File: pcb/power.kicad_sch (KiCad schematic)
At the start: 6 parts

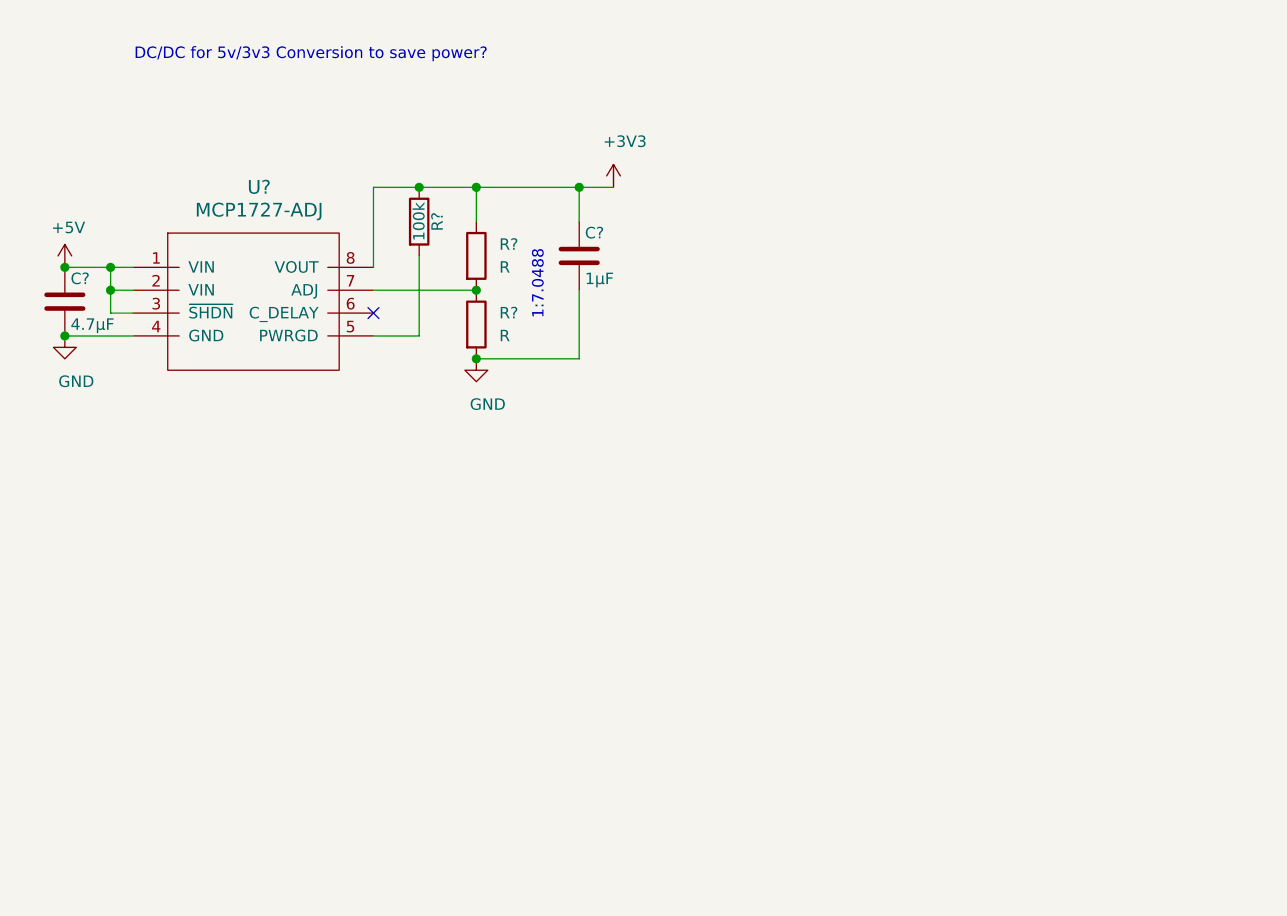
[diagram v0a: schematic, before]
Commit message: refinements; add ar1335 footprint
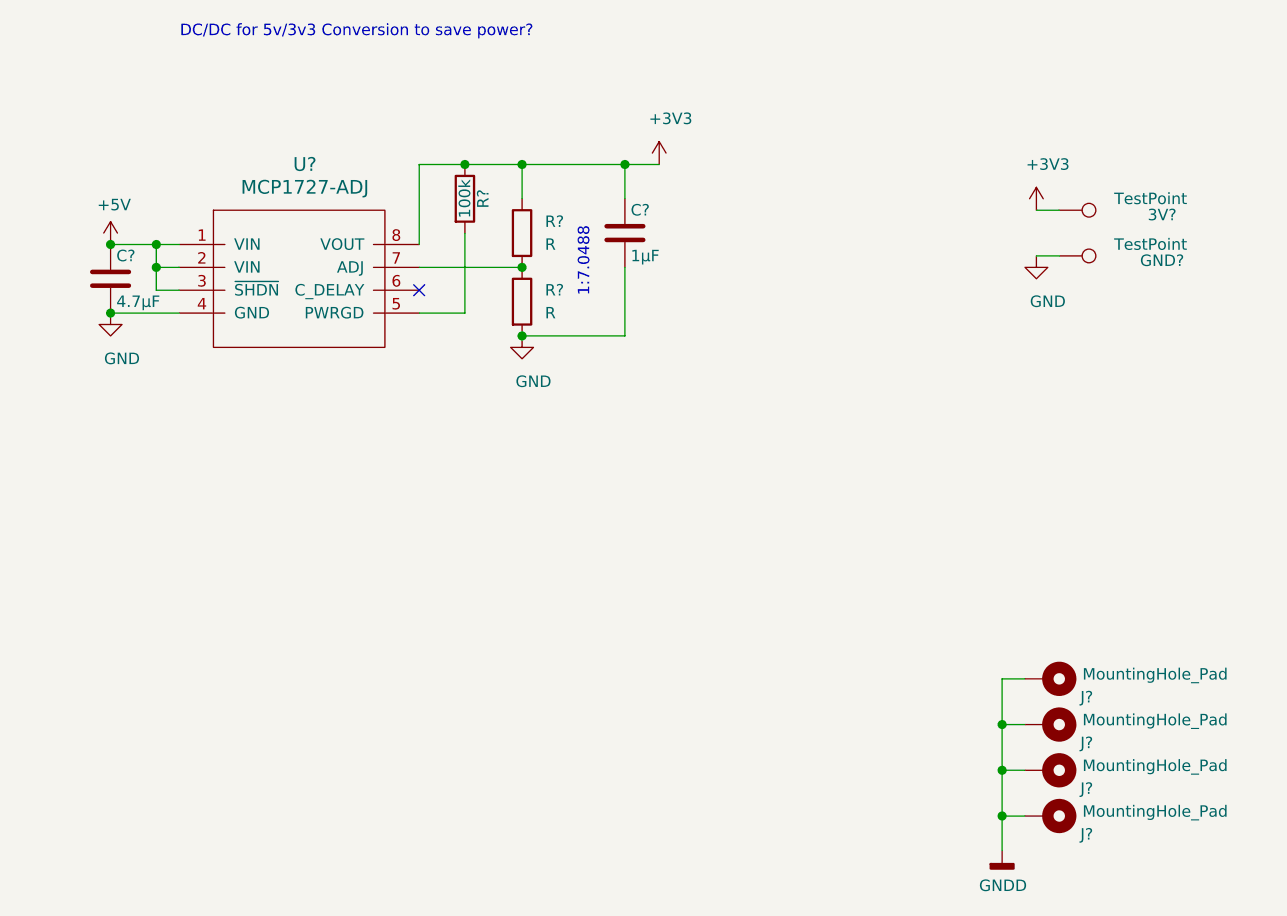
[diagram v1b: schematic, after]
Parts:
- added 3V?, GND?: TestPoint, Connectors_TestPoints:Test_Point_Pad_2.0x2.0mm, symbol Connector:TestPoint
- added J? (x4): MountingHole_Pad, Mounting_Holes:MountingHole_3.2mm_M3_Pad, symbol Mechanical:MountingHole_Pad
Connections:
- net +3V3: now also 3V?.1
- net GND: now also GND?.1
- new net GNDD: J?.1, J?.1, J?.1, J?.1
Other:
- moved on the sheet: C?, R?, U?

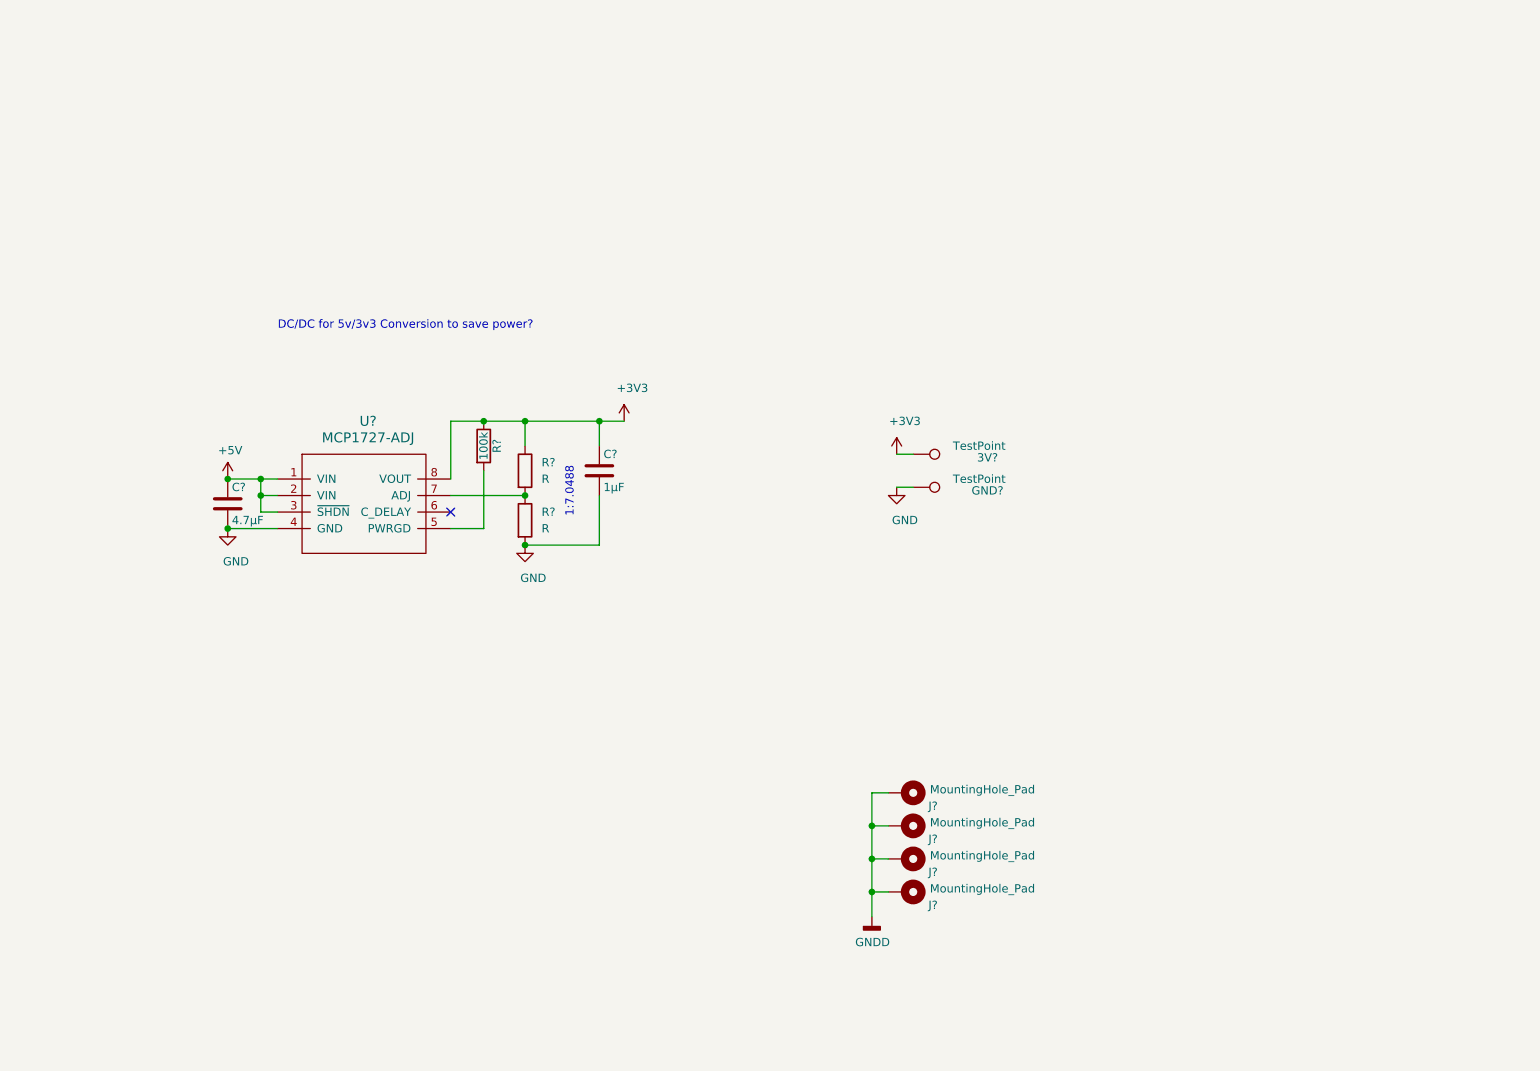
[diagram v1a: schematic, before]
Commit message: Change Plans: two image sensors
* Redo power management
* Add level shifters
* Intention to use both image sensors on the same board
* Add Pmod & LEDs
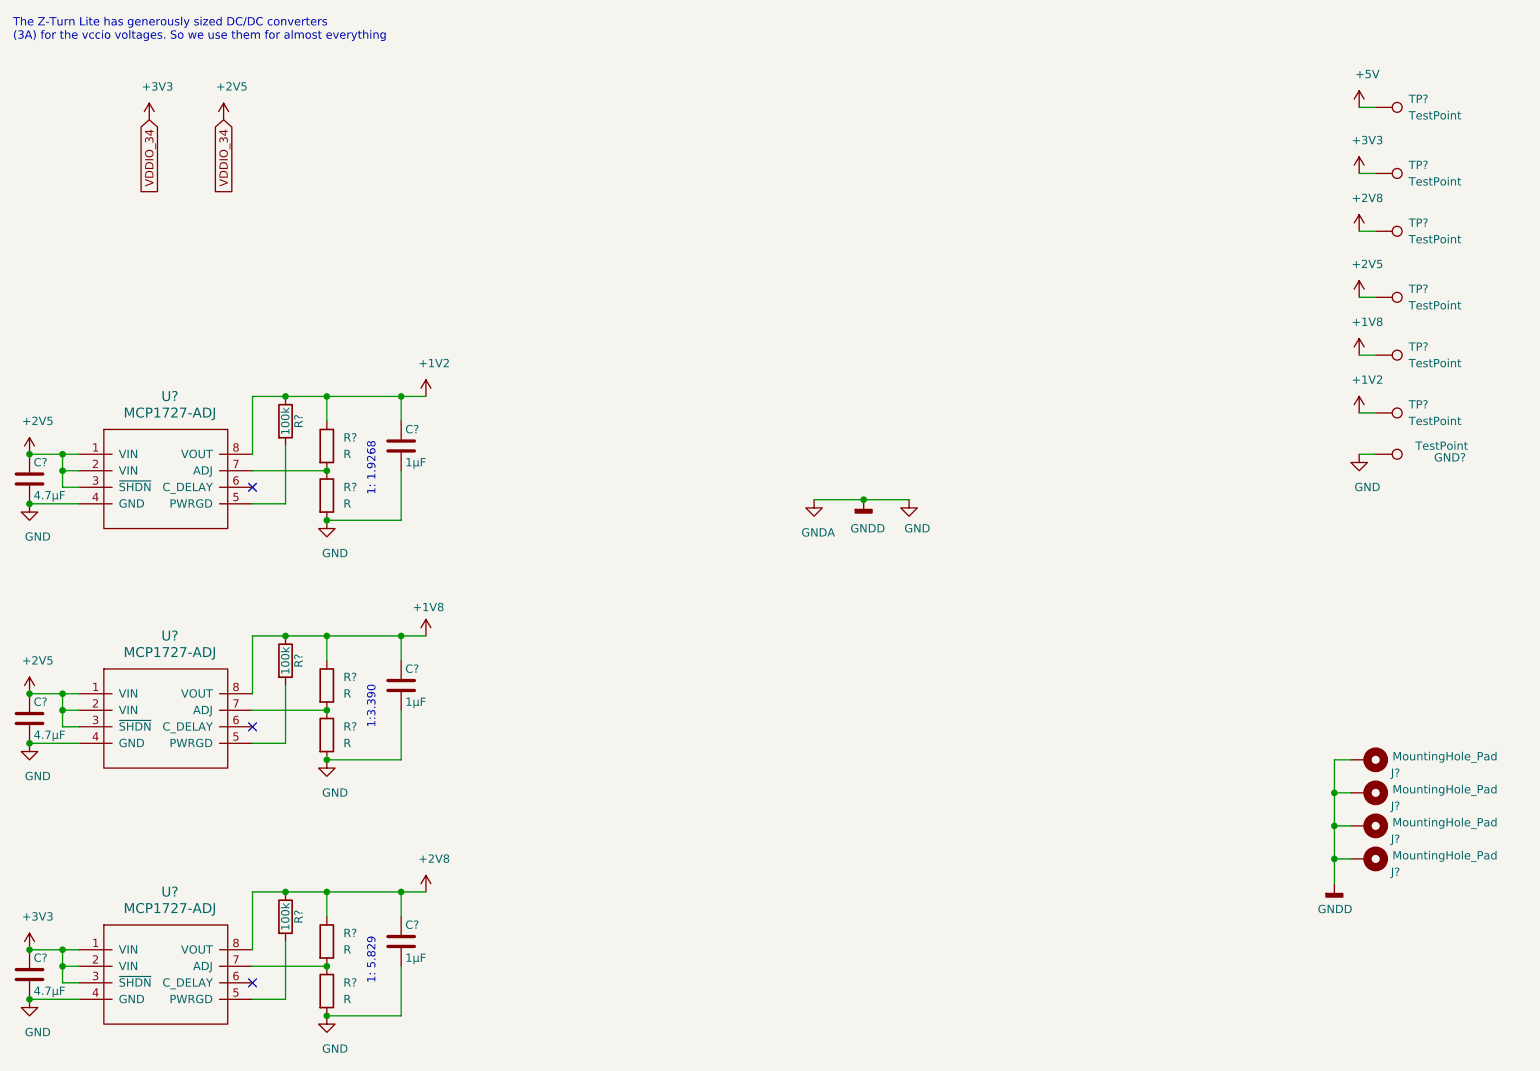
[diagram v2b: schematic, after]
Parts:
- removed 3V?: TestPoint, Connectors_TestPoints:Test_Point_Pad_2.0x2.0mm, symbol Connector:TestPoint
- removed C?: 4.7µF, Capacitors_SMD:C_0603_HandSoldering, symbol Device:C
- removed C?: 1µF, Capacitors_SMD:C_0402, symbol Device:C
- removed R?: 100k, Resistors_SMD:R_0603_HandSoldering, symbol Device:R
- removed R? (x2): R, symbol Device:R
- removed U?: MCP1727-ADJ, symbol parts:MCP1727-ADJ
- added C? (x3): 4.7µF, Capacitors_SMD:C_0603_HandSoldering, symbol Device:C
- added C? (x3): 1µF, Capacitors_SMD:C_0402, symbol Device:C
- added R? (x6): R, symbol Device:R
- added R? (x3): 100k, Resistors_SMD:R_0603_HandSoldering, symbol Device:R
- added TP? (x6): TestPoint, symbol Connector:TestPoint
- added U? (x3): MCP1727-ADJ, symbol parts:MCP1727-ADJ
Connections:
- net GNDD is gone; now on net GND: J?.1, J?.1, J?.1, J?.1
- net +5V: now also TP?.1
- net GND: now also C?.2, C?.2, C?.2, C?.2, C?.2, C?.2, R?.2, R?.2, R?.2, U?.4 (GND), U?.4 (GND), U?.4 (GND)
- new net: R?.1, R?.2, U?.7 (ADJ) (x3)
- new net: R?.2, U?.5 (PWRGD) (x3)
- new net +1V2: C?.1, R?.1, R?.1, TP?.1, U?.8 (VOUT)
- new net +1V8: C?.1, R?.1, R?.1, TP?.1, U?.8 (VOUT)
- new net +2V5: C?.1, C?.1, C?.1, TP?.1, TP?.1, U?.1 (VIN), U?.1 (VIN), U?.1 (VIN), U?.2 (VIN), U?.2 (VIN), U?.2 (VIN), U?.3 (~SHDN), U?.3 (~SHDN), U?.3 (~SHDN)
- new net +2V8: C?.1, R?.1, R?.1, TP?.1, U?.8 (VOUT)
- no-connect marks 1 -> 3
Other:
- note added: "1: 1.9268"
- note added: "1: 5.829"
- note added: "1:3.390"
- note added: "The Z-Turn Lite has generously sized DC/DC converters (3A) for the vccio voltages. So we use them for almost everything"
- note removed: "1:7.0488"
- note removed: "DC/DC for 5v/3v3 Conversion to save power?"
- moved on the sheet: GND?, J?
